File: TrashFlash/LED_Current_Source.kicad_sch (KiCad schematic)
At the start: 22 parts, among them IC3 OPA191IDBVR, Q1 BC56-10PA,115, Q2 BC56-10PA,115, Q3 BC56-10PA,115, Q4 BC56-10PA,115

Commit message: Started redrawing shematic
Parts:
- added R18: 10m, symbol Device:R
- C1, C2: value 10p -> 22p
- R1, R2, R3, R4: value 50m -> 68m; footprint (none) -> Resistor_SMD:R_0603_1608Metric
- R5: value 10m -> 1
- R6, R7: value 10k -> 12k
- R8, R9: value 100k -> 150k
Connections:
- net GND: no longer D1.1 (K)
- net V_LED: now also D4.2 (A); no longer Q1.3 (C), Q2.3 (C), Q3.3 (C), Q4.3 (C)
- net at R1.2, R2.2, R3.2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: now also R18.1
- net at IC3.3 (+), R9.2: now also C2.2, R7.2; no longer C2.1, R7.1
- new net: D1.1 (K), Q1.3 (C), Q2.3 (C), Q3.3 (C), Q4.3 (C)
- now unconnected: R5.2
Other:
- moved on the sheet: C1, C2, C3, C4, D1, D2, D3, D4, IC3A, IC3B, Q1, Q2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

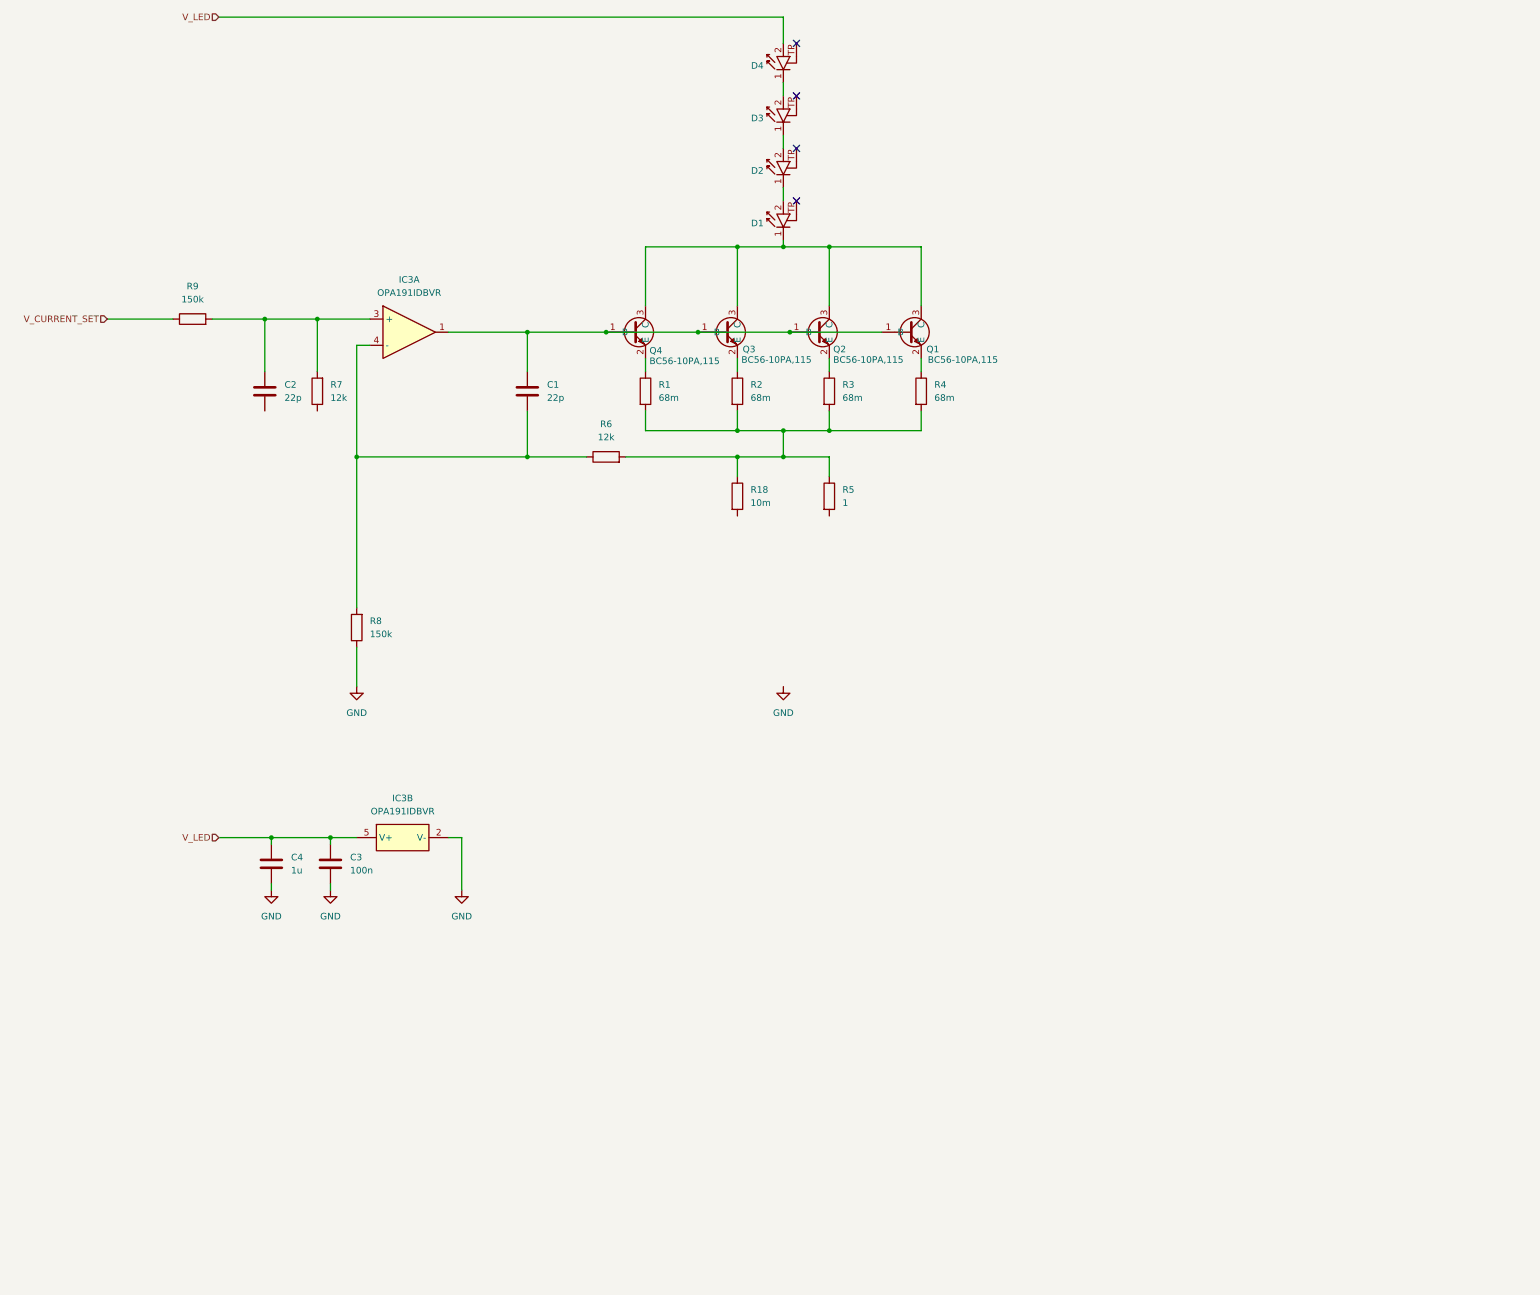
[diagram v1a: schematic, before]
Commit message: LED_Current_Source.kicad_sch redesigne
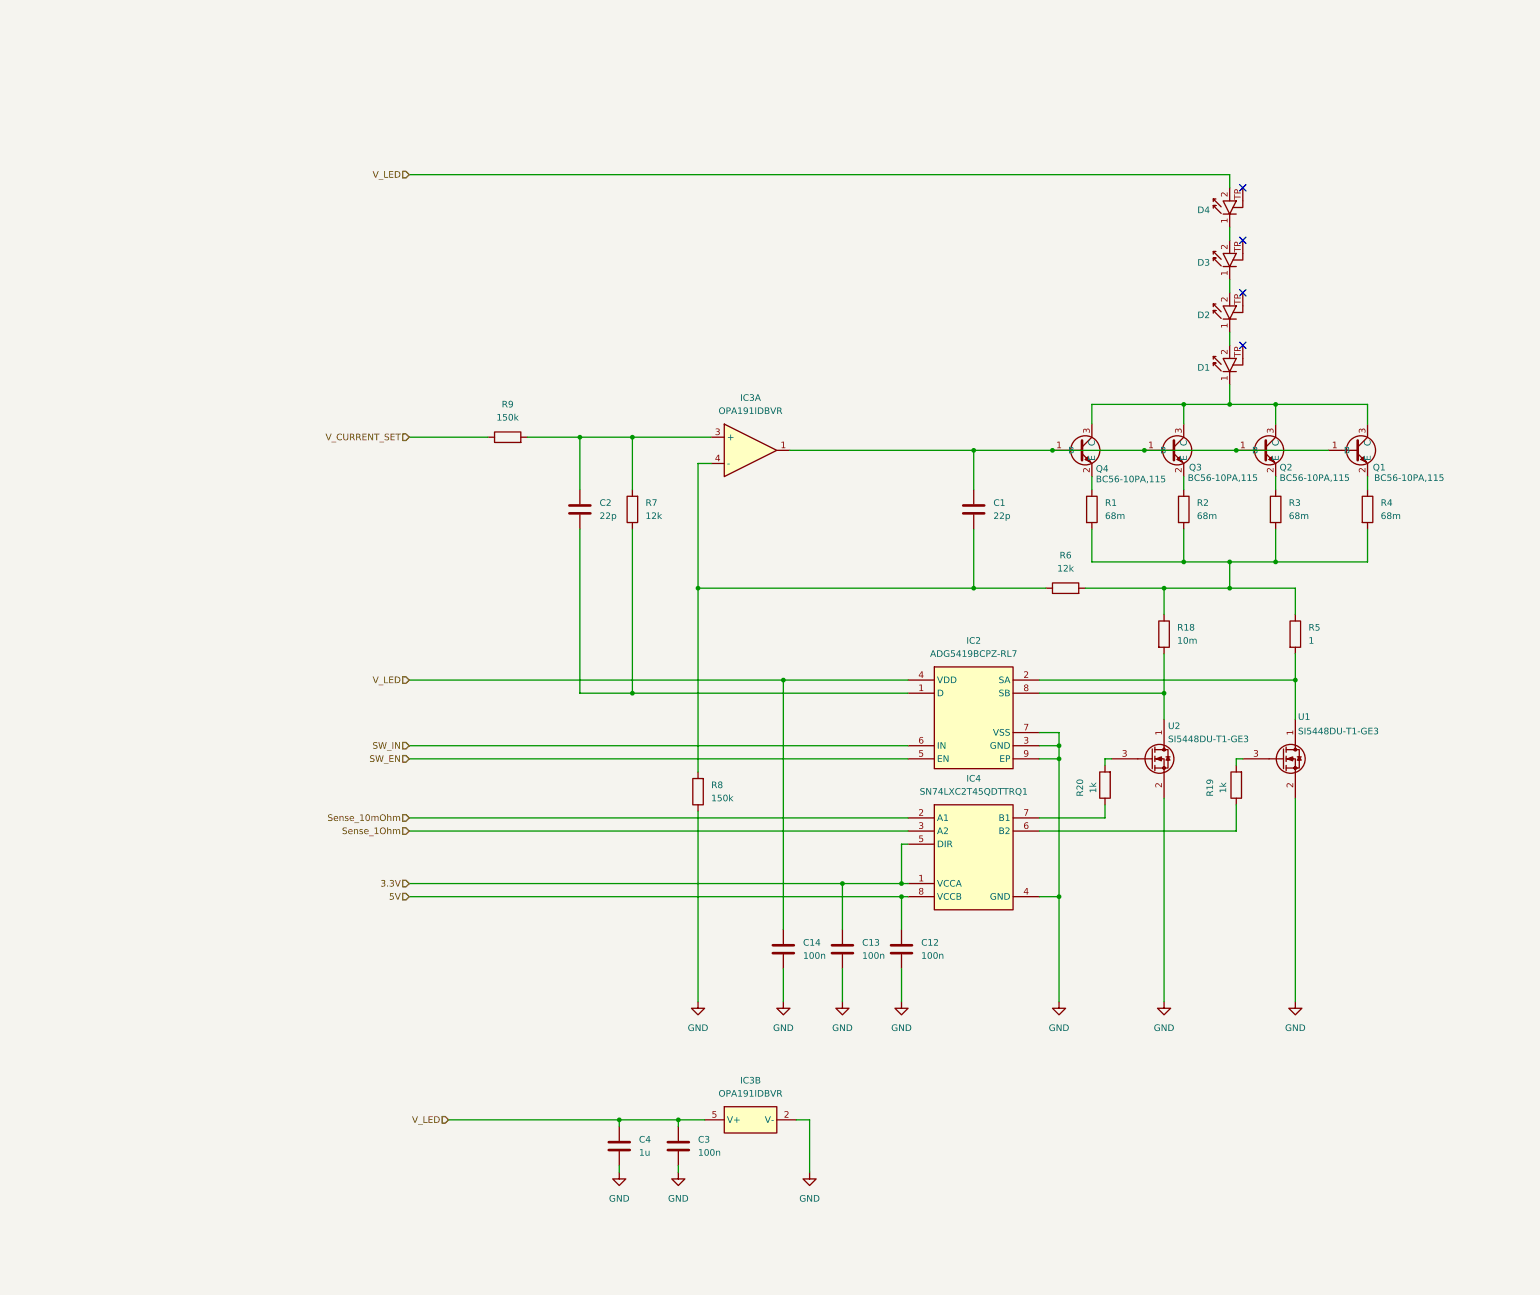
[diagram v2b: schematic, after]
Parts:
- added C12, C13, C14: 100n, symbol Device:C
- added IC2: ADG5419BCPZ-RL7, SON50P300X200X80-9N-D, symbol TrashFlash:ADG5419BCPZ-RL7
- added IC4: SN74LXC2T45QDTTRQ1, SN74LXC2T45QDTTRQ1, symbol TrashFlash:SN74LXC2T45QDTTRQ1
- added R19, R20: 1k, symbol Device:R
- added U1, U2: SI5448DU-T1-GE3, SI5448DUT1GE3, symbol TrashFlash:SI5448DU-T1-GE3
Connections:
- net GND: now also C12.2, C13.2, C14.2, IC2.3 (GND), IC2.7 (VSS), IC2.9 (EP), IC4.4 (GND), U1.2, U2.2
- net V_LED: now also C14.1, IC2.4 (VDD)
- net at R18.2: now also IC2.8 (SB), U2.1
- net at R5.2: now also IC2.2 (SA), U1.1
- net at C2.1: now also R7.1, IC2.1 (D)
- new net: R20.2, U2.3
- new net: IC4.6 (B2), R19.1
- new net: R19.2, U1.3
- new net: IC4.7 (B1), R20.1
- new net 3.3V: C13.1, IC4.1 (VCCA), IC4.5 (DIR)
- new net 5V: C12.1, IC4.8 (VCCB)
- new net SW_EN: IC2.5 (EN)
- new net SW_IN: IC2.6 (IN)
- new net Sense_10mOhm: IC4.2 (A1)
- new net Sense_1Ohm: IC4.3 (A2)
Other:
- moved on the sheet: C1, C2, C3, C4, D1, D2, D3, D4, IC3A, IC3B, Q1, Q2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

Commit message: Cleaned up LED_Current_Source schematic
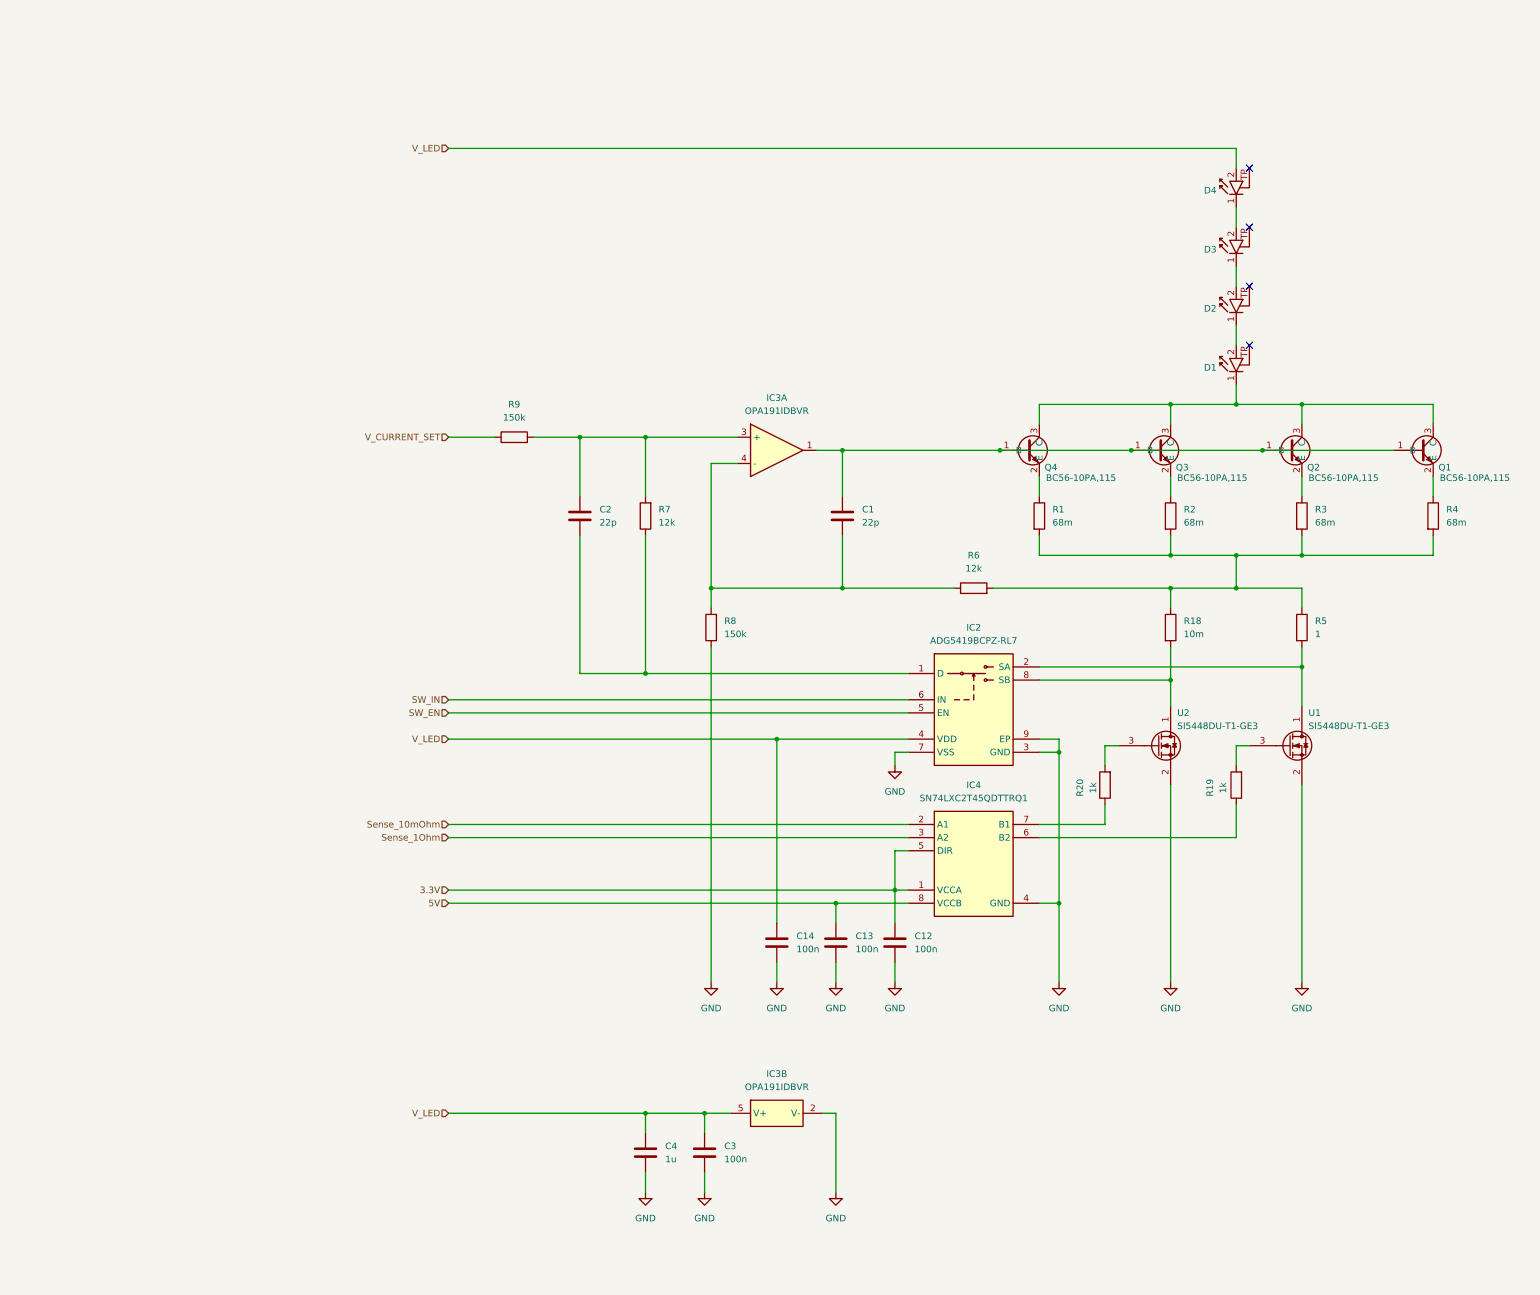
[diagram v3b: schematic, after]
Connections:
- net 3.3V: now also C12.1; no longer C13.1
- net 5V: now also C13.1; no longer C12.1
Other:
- moved on the sheet: C1, C12, C13, C14, C2, C3, C4, D1, D2, D3, D4, IC3A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

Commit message: Added comment
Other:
- note added: "AD8615!"
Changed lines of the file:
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@@
 	(generator_version "9.0")
 	(paper "A3")
+	(text "AD8615!\n"
+		(exclude_from_sim no)
+		(at 184.15 85.852 0)
+		(effects
+			(font
+				(size 2.54 2.54)
+				(color 255 0 0 1)
+			)
+			(justify left)
+		)
+	)
 	(junction
 		(at 233.68 100.33)

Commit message: Added Battery Management
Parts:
- removed IC3: OPA191IDBVR, SOT95P280X145-5N, symbol TrashFlash:OPA191IDBVR
- added IC8: AD8615AUJZ-REEL, SOT95P280X100-5N, symbol TrashFlash:AD8615AUJZ-REEL
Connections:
- net GND: now also IC8.2 (V-)
- net V_LED: now also IC8.5 (V+)
- net at C1.2, R6.1, R8.2: now also IC8.4 (-)
- net at C1.1, Q1.1 (B), Q2.1 (B)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: now also IC8.1
- net at C2.2, R7.2, R9.2: now also IC8.3 (+)
- net 3.3V renamed VDD
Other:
- note removed: "AD8615!"

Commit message: Added USB and powernets
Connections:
- net at IC4.6 (B2), R19.1: now also R19.2, U1.3
- net 5V renamed +5V
- net +5V: now also C3.2, C4.2, IC8.5 (V+)
- net Sense_10mOhm renamed EN_20A_PATH
- net Sense_1Ohm renamed EN_0.2A_PATH
- net V_LED renamed Vdrive
- net Vdrive: no longer C3.2, C4.2, IC8.5 (V+)
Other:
- moved on the sheet: C1, C12, C13, C14, C2, C3, C4, D1, D2, D3, D4, IC2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

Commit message: Rotary encoder added + 3D stuff
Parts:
- C1, C12, C13, C14, C2, C3: footprint (none) -> Capacitor_SMD:C_0402_1005Metric
- C4: footprint (none) -> Capacitor_SMD:C_0603_1608Metric
- IC2: footprint SON50P300X200X80-9N-D -> TrashFlash:SON50P300X200X80-9N-D
- IC4: footprint SN74LXC2T45QDTTRQ1 -> TrashFlash:SN74LXC2T45QDTTRQ1
- IC8: footprint SOT95P280X100-5N -> TrashFlash:SOT95P280X100-5N
- Q1, Q2, Q3, Q4: footprint PTVS24VZ1UPAZ -> TrashFlash:PTVS24VZ1UPAZ
- R18, R5: footprint (none) -> Resistor_SMD:R_0603_1608Metric
- R19, R20, R6, R7, R8, R9: footprint (none) -> Resistor_SMD:R_0402_1005Metric
- U1, U2: footprint SI5448DUT1GE3 -> TrashFlash:SI5448DUT1GE3
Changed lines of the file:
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@@
 			)
 		)
-		(property "Footprint" "SI5448DUT1GE3"
+		(property "Footprint" "TrashFlash:SI5448DUT1GE3"
 			(at 285.75 235.89 0)
 			(effects
@@
 			)
 		)
-		(property "Footprint" ""
+		(property "Footprint" "Capacitor_SMD:C_0402_1005Metric"
 			(at 201.6252 208.28 0)
 			(effects
@@
 			)
 		)
-		(property "Footprint" ""
+		(property "Footprint" "Resistor_SMD:R_0402_1005Metric"
 			(at 226.06 112.268 90)
 			(effects
@@
 			)
 		)
-		(property "Footprint" ""
+		(property "Footprint" "Capacitor_SMD:C_0603_1608Metric"
 			(at 161.5948 243.84 0)
 			(effects
@@
 			)
 		)
-		(property "Footprint" "SON50P300X200X80-9N-D"
+		(property "Footprint" "TrashFlash:SON50P300X200X80-9N-D"
 			(at 226.314 145.796 0)
 			(effects
@@
 			)
 		)
-		(property "Footprint" "SOT95P280X100-5N"
+		(property "Footprint" "TrashFlash:SOT95P280X100-5N"
 			(at 209.55 334.95 0)
 			(effects
@@
 			)
 		)
-		(property "Footprint" ""
+		(property "Footprint" "Capacitor_SMD:C_0402_1005Metric"
 			(at 213.0552 208.28 0)
 			(effects
@@
 			)
 		)
-		(property "Footprint" "PTVS24VZ1UPAZ"
+		(property "Footprint" "TrashFlash:PTVS24VZ1UPAZ"
 			(at 262.636 96.774 0)
 			(effects
@@
 			)
 		)
-		(property "Footprint" ""
+		(property "Footprint" "Capacitor_SMD:C_0402_1005Metric"
 			(at 201.6252 152.4 0)
 			(effects
@@
 			)
 		)
-		(property "Footprint" ""
+		(property "Footprint" "Resistor_SMD:R_0402_1005Metric"
 			(at 278.638 148.59 90)
 			(effects
@@
 			)
 		)
-		(property "Footprint" ""
+		(property "Footprint" "Resistor_SMD:R_0402_1005Metric"
 			(at 137.16 83.058 90)
 			(effects
@@
 			)
 		)
-		(property "Footprint" ""
+		(property "Footprint" "Resistor_SMD:R_0402_1005Metric"
 			(at 253.238 148.59 90)
 			(effects
@@
 			)
 		)
-		(property "Footprint" ""
+		(property "Footprint" "Resistor_SMD:R_0402_1005Metric"
 			(at 177.038 118.11 90)
 			(effects
@@
 			)
 		)
-		(property "Footprint" "PTVS24VZ1UPAZ"
+		(property "Footprint" "TrashFlash:PTVS24VZ1UPAZ"
 			(at 313.436 96.774 0)
 			(effects
@@
 			)
 		)
-		(property "Footprint" "SOT95P280X100-5N"
+		(property "Footprint" "TrashFlash:SOT95P280X100-5N"
 			(at 207.01 178.74 0)
 			(effects
@@
 			)
 		)
-		(property "Footprint" "SN74LXC2T45QDTTRQ1"
+		(property "Footprint" "TrashFlash:SN74LXC2T45QDTTRQ1"
 			(at 251.46 273.99 0)
 			(effects
@@
 			)
 		)
-		(property "Footprint" ""
+		(property "Footprint" "Resistor_SMD:R_0603_1608Metric"
 			(at 262.382 118.11 90)
 			(effects
@@
 			)
 		)
-		(property "Footprint" ""
+		(property "Footprint" "Capacitor_SMD:C_0402_1005Metric"
 			(at 201.6252 100.33 0)
 			(effects
@@
 			)
 		)
-		(property "Footprint" ""
+		(property "Footprint" "Capacitor_SMD:C_0402_1005Metric"
 			(at 173.0248 243.84 0)
 			(effects
@@
 			)
 		)
-		(property "Footprint" "PTVS24VZ1UPAZ"
+		(property "Footprint" "TrashFlash:PTVS24VZ1UPAZ"
 			(at 237.236 96.774 0)
 			(effects
@@
 			)
 		)
-		(property "Footprint" "PTVS24VZ1UPAZ"
+		(property "Footprint" "TrashFlash:PTVS24VZ1UPAZ"
 			(at 288.036 96.774 0)
 			(effects
@@
 			)
 		)
-		(property "Footprint" ""
+		(property "Footprint" "Resistor_SMD:R_0603_1608Metric"
 			(at 287.782 118.11 90)
 			(effects
@@
 			)
 		)
-		(property "Footprint" ""
+		(property "Footprint" "Capacitor_SMD:C_0402_1005Metric"
 			(at 148.8948 92.71 0)
 			(effects
@@
 			)
 		)
-		(property "Footprint" "SI5448DUT1GE3"
+		(property "Footprint" "TrashFlash:SI5448DUT1GE3"
 			(at 311.15 235.89 0)
 			(effects
@@
 			)
 		)
-		(property "Footprint" ""
+		(property "Footprint" "Resistor_SMD:R_0402_1005Metric"
 			(at 164.338 96.52 90)
 			(effects

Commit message: Footprints 3D model fixed
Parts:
- IC2: footprint TrashFlash:SON50P300X200X80-9N-D -> SON50P300X200X80-9N-D
- IC4: footprint TrashFlash:SN74LXC2T45QDTTRQ1 -> SN74LXC2T45QDTTRQ1
- IC8: footprint TrashFlash:SOT95P280X100-5N -> SOT95P280X100-5N
- Q1, Q2, Q3, Q4: footprint TrashFlash:PTVS24VZ1UPAZ -> PTVS24VZ1UPAZ
- U1, U2: footprint TrashFlash:SI5448DUT1GE3 -> SI5448DUT1GE3
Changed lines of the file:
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@@
 			)
 		)
-		(property "Footprint" "TrashFlash:SI5448DUT1GE3"
+		(property "Footprint" "SI5448DUT1GE3"
 			(at 285.75 235.89 0)
 			(effects
@@
 			)
 		)
-		(property "Footprint" "TrashFlash:SON50P300X200X80-9N-D"
+		(property "Footprint" "SON50P300X200X80-9N-D"
 			(at 226.314 145.796 0)
 			(effects
@@
 			)
 		)
-		(property "Footprint" "TrashFlash:SOT95P280X100-5N"
+		(property "Footprint" "SOT95P280X100-5N"
 			(at 209.55 334.95 0)
 			(effects
@@
 			)
 		)
-		(property "Footprint" "TrashFlash:PTVS24VZ1UPAZ"
+		(property "Footprint" "PTVS24VZ1UPAZ"
 			(at 262.636 96.774 0)
 			(effects
@@
 			)
 		)
-		(property "Footprint" "TrashFlash:PTVS24VZ1UPAZ"
+		(property "Footprint" "PTVS24VZ1UPAZ"
 			(at 313.436 96.774 0)
 			(effects
@@
 			)
 		)
-		(property "Footprint" "TrashFlash:SOT95P280X100-5N"
+		(property "Footprint" "SOT95P280X100-5N"
 			(at 207.01 178.74 0)
 			(effects
@@
 			)
 		)
-		(property "Footprint" "TrashFlash:SN74LXC2T45QDTTRQ1"
+		(property "Footprint" "SN74LXC2T45QDTTRQ1"
 			(at 251.46 273.99 0)
 			(effects
@@
 			)
 		)
-		(property "Footprint" "TrashFlash:PTVS24VZ1UPAZ"
+		(property "Footprint" "PTVS24VZ1UPAZ"
 			(at 237.236 96.774 0)
 			(effects
@@
 			)
 		)
-		(property "Footprint" "TrashFlash:PTVS24VZ1UPAZ"
+		(property "Footprint" "PTVS24VZ1UPAZ"
 			(at 288.036 96.774 0)
 			(effects
@@
 			)
 		)
-		(property "Footprint" "TrashFlash:SI5448DUT1GE3"
+		(property "Footprint" "SI5448DUT1GE3"
 			(at 311.15 235.89 0)
 			(effects
